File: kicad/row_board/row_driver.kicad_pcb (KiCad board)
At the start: 2 copper layers, 100 x 100 mm, 80 parts, among them J1 Panel row connector (female), J2 Row daisy chain connector (ma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, J3 Conn_01x04, J4 Column Board Connector, J6 Barrel_Jack, J7 Controller A, J8 Controller B, Q1 2N3904, Q2 FQP47P06, U1 TPIC6B595, U11 ArduinoNanoR3, U12 WeMos_mini, U13 TXB0108-PWR, U2 TPIC6B595, U3 TBD62783, U4 TPIC6B595, U5 TPIC6B595, U6 TBD62783, U7 WE-FDSM_DC/DC_5V, U8 4N25

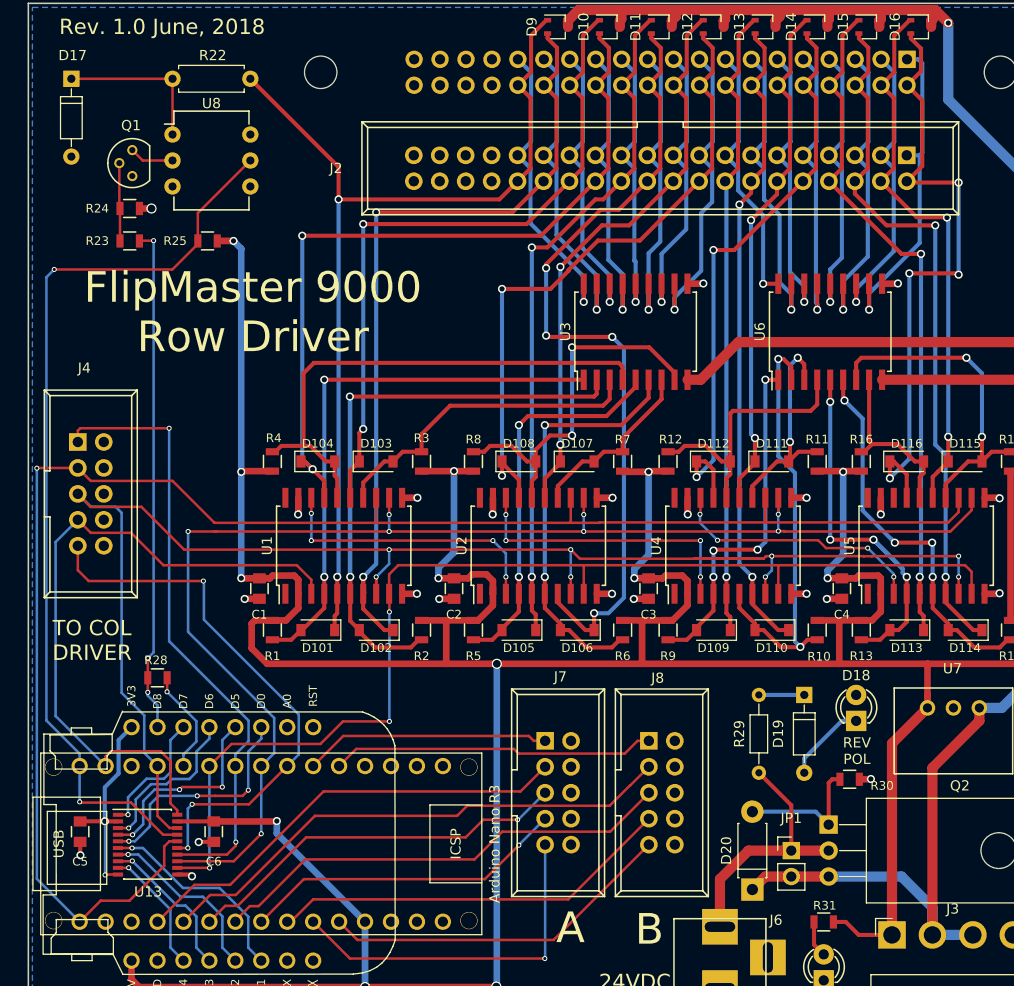
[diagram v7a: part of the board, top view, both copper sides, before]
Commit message: Fully routed row board
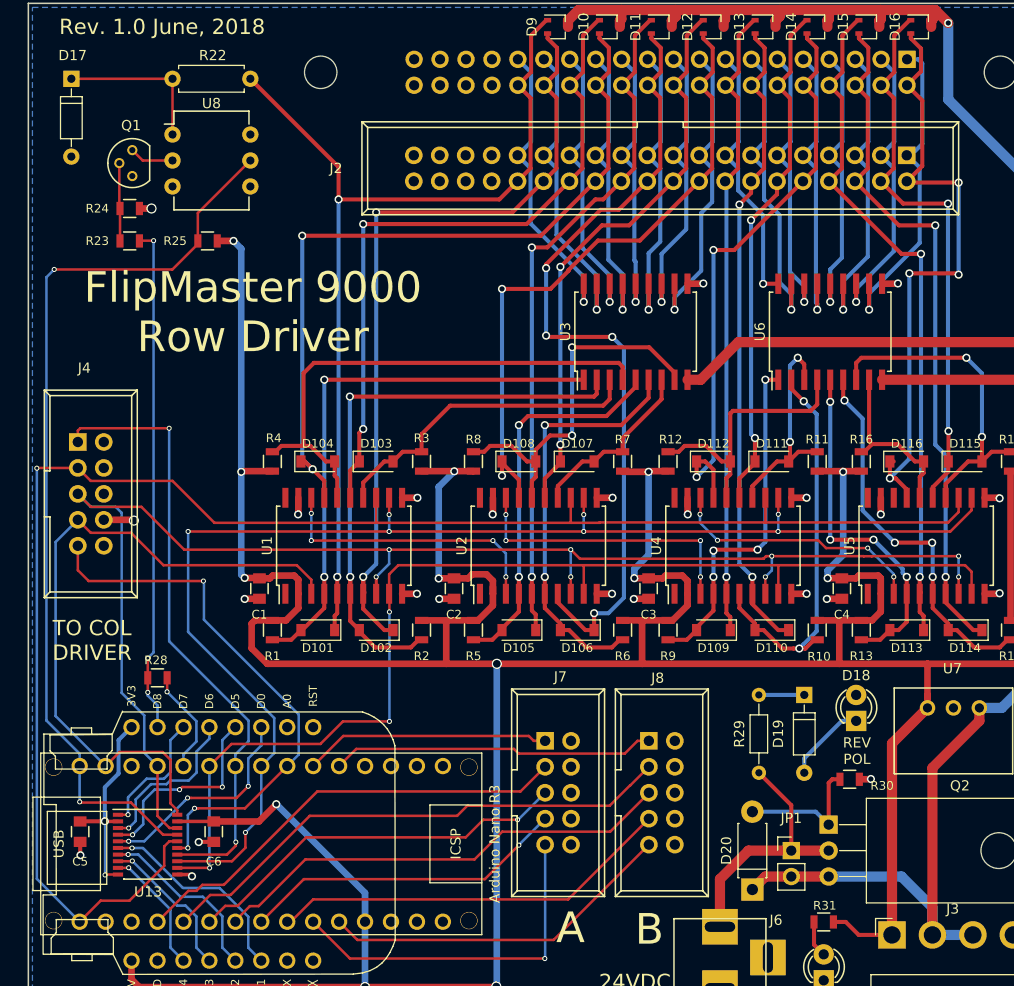
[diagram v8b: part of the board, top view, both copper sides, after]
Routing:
- net Net-(D102-Pad2): track 75.4 -> 57.8 mm
- net ~RC_CLEAR: track 153.1 -> 146.0 mm
- net Net-(D113-Pad2): track 38.6 -> 34.6 mm
- net Net-(D110-Pad2): track 43.4 -> 39.4 mm
- net GND: track 34.1 -> 37.1 mm, vias 23 -> 24
- net ROW_REG_CLK: track 133.5 -> 131.6 mm
- net +5V: track 391.3 -> 393.3 mm
- net ROW4_L: track 68.6 -> 67.0 mm
- net ROW8_L: track 63.9 -> 62.2 mm
- net ROW6_L: track 52.6 -> 50.9 mm
- net RC_SHIFT_CLK_3v3: track 22.8 -> 21.3 mm
- net ROW2_L: track 53.9 -> 55.0 mm
- net ROW1_L: track 62.8 -> 61.6 mm
- net ROW3_L: track 68.8 -> 68.1 mm
- net RC_DATA: track 67.1 -> 66.6 mm
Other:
- rule trace_min: 0.09 -> 0.1
- rule via_min_size: 0.45 -> 0.5
